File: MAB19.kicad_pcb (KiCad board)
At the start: 2 copper layers, 84 parts, among them J1 Screw_Terminal_01x02, J2 Screw_Terminal_01x03, J401 USART, J601 RJ45, J602 RJ45, K1 coil: 12VDC, contact: 125V/10A, Q1 BCV27, U1 4N25, U201 MCP2551-I/SN, U202 MCP2515-xSO, U401 ATMEGA328P-PU, U501 LM7805, Y201 16MHz, Y401 16MHz

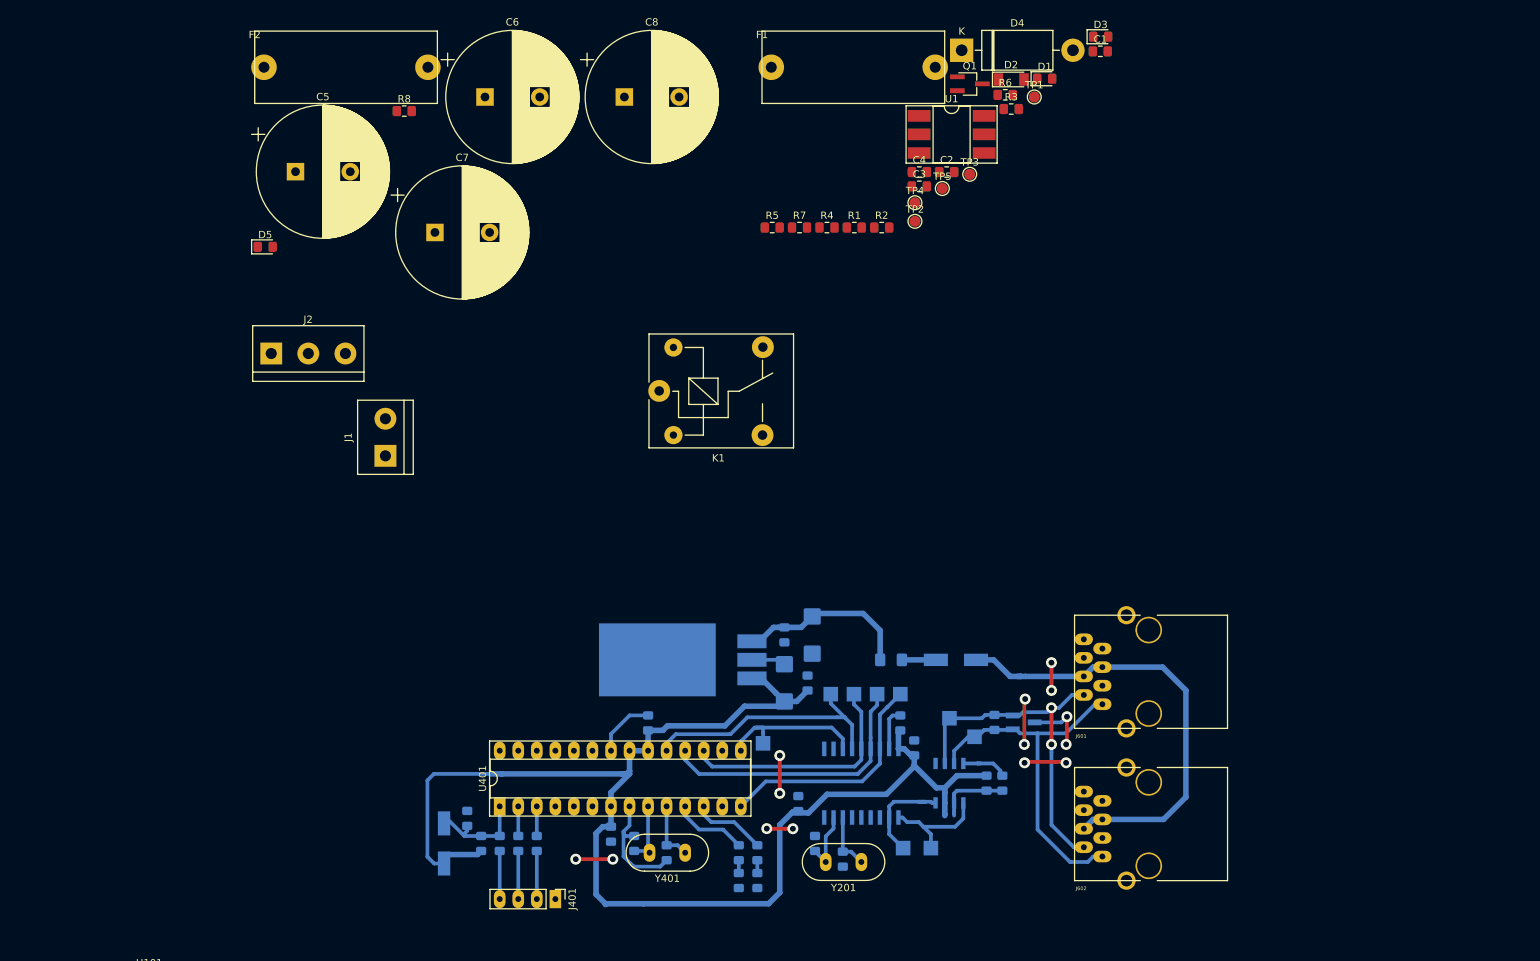
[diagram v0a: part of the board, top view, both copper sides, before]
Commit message: Adicionado safe zone para separar os GNDs
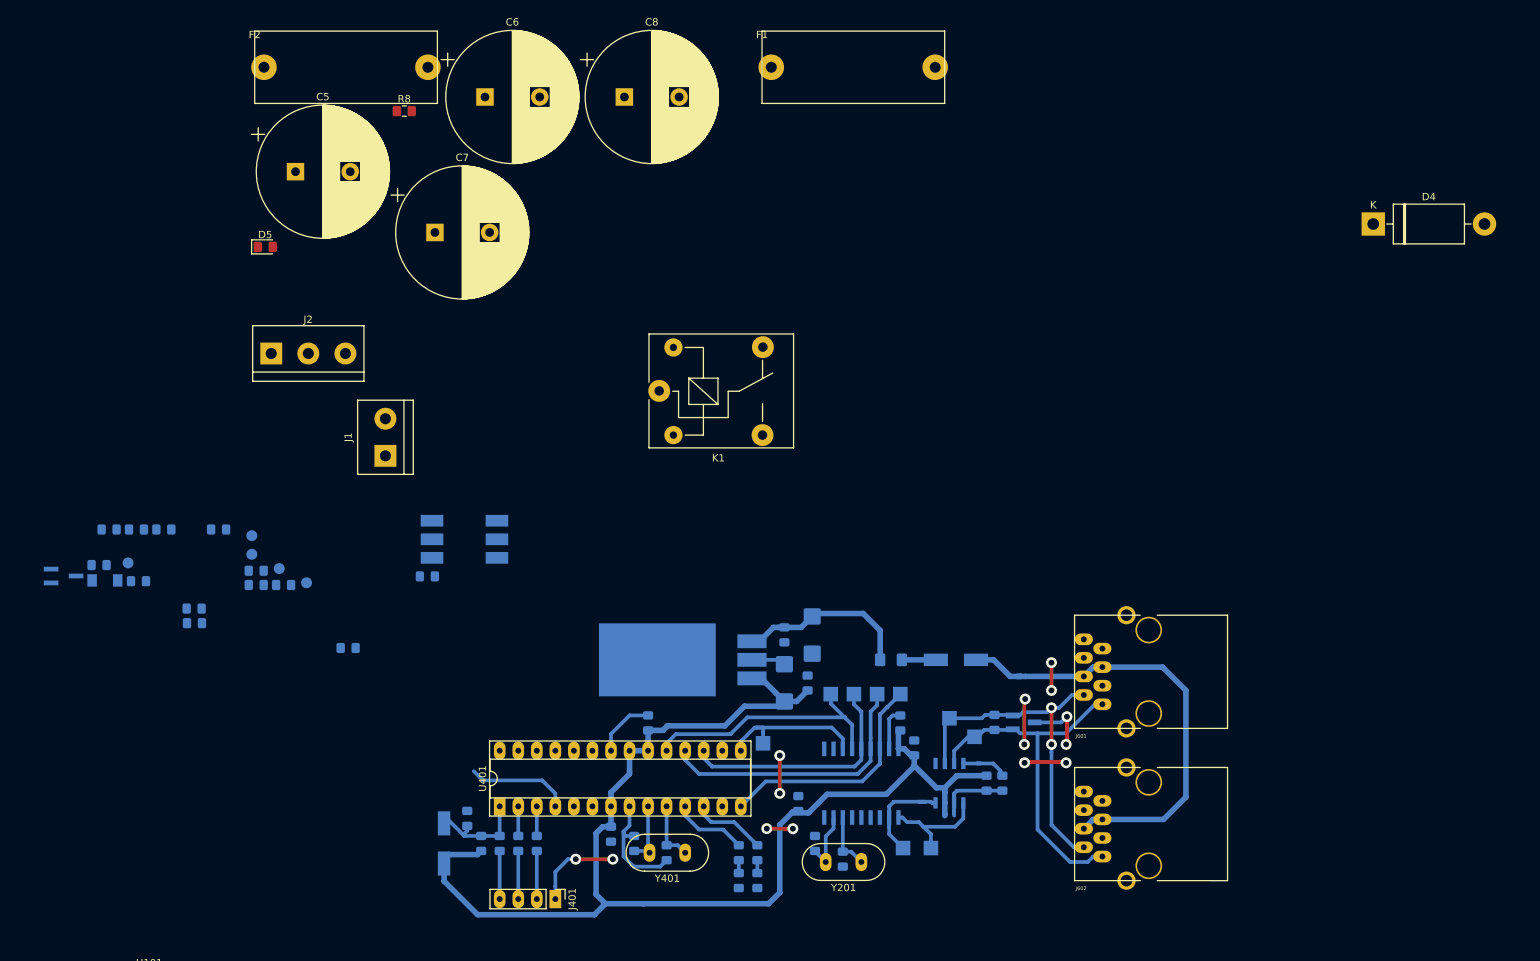
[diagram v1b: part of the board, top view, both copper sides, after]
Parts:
- C1, C2, C3, C4, D1, D2, D3, Q1, R1, R2, R3, R4, R5, R6, R7, TP1, TP2, TP3, TP4, TP5, U1: moved to B.Cu
- moved D3 147.8 mm to (68.4, 82.6)
- moved C1 145.7 mm to (68.4, 80.6)
- moved D1 141.9 mm to (60.8, 76.9)
- moved D2 141.8 mm to (56.2, 76.7)
- moved Q1 141.2 mm to (50.5, 76.1)
- moved R6 139.8 mm to (55.4, 74.6)
- moved TP1 139.5 mm to (59.3, 74.3)
- moved R3 117.0 mm to (89.5, 86.0)
- moved C2 107.0 mm to (80.6, 77.4)
- moved C4 107.0 mm to (76.9, 77.4)
- moved TP3 106.7 mm to (83.8, 77.1)
- moved C3 105.0 mm to (76.9, 75.4)
- moved TP5 104.7 mm to (80.0, 75.1)
- moved TP4 102.8 mm to (76.3, 73.2)
- moved TP2 100.5 mm to (76.3, 70.6)
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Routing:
- net +5V: track 187.6 -> 170.6 mm
- net /MCU/ON_OFF_PUMP: track 0.00 -> 14.2 mm
- net GND: track 79.5 -> 86.8 mm

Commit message: Pequena alteeração
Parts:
- moved TP1 62.8 mm to (119.4, 92.7)
- moved TP2 51.9 mm to (121.9, 95.2)
- moved C1 50.6 mm to (116.8, 95.2), turned to 270 degrees
- moved R1 20.0 mm to (105.4, 95.5), turned to 270 degrees
- moved U1 18.9 mm to (111.8, 88.9), turned to 90 degrees
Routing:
- net Net-(C1-Pad1): track 0.00 -> 21.7 mm
- net GND: track 86.8 -> 106.8 mm
- net /MCU/ON_OFF_PUMP: track 14.2 -> 21.1 mm
- added copper zone on B.Cu, net GND

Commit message: First version PCB
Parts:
- added JP1: SolderJumper_3_Bridged12, Jumper:SolderJumper-3_P1.3mm_Bridged2Bar12_Pad1.0x1.5mm_NumberLabels, B.Cu at (118.1, 64.1)
- D5, R8: moved to B.Cu
- moved F2 133.6 mm to (200.7, 51.2), turned to 180 degrees
- moved D5 125.9 mm to (202.6, 50.2), turned to 90 degrees
- moved R8 113.5 mm to (202.6, 54.6), turned to 90 degrees
- moved D4 102.6 mm to (128.9, 46.4), turned to 180 degrees
- moved C5 101.0 mm to (172.5, 66.0), turned to 90 degrees
- moved C8 86.0 mm to (193.0, 66.0), turned to 90 degrees
- moved C7 62.7 mm to (152.0, 66.0), turned to 90 degrees
- moved C6 60.2 mm to (131.4, 66.0), turned to 90 degrees
- moved Q1 58.5 mm to (106.7, 59.7)
- moved F1 56.1 mm to (172.1, 51.2), turned to 180 degrees
- moved R6 51.1 mm to (102.9, 55.9), turned to 90 degrees
- moved J1 49.2 mm to (141.0, 43.2), turned to 180 degrees
- moved D3 48.1 mm to (104.1, 50.4), turned to 90 degrees
- moved D2 47.3 mm to (101.0, 61.6), turned to 90 degrees
- moved R5 44.6 mm to (101.0, 75.3), turned to 270 degrees
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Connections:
- net /POWER SUPPLY/+18V_OUT renamed Net-(C501-Pad1)
- J1 pad 1: GNDPWR -> /filter/Vin
- J1 pad 2: /filter/Vin -> GNDPWR
- K1 pad 3: /pump_driver/+Pump -> Net-(JP1-Pad1)
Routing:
- net GNDPWR: track 0.00 -> 201.2 mm
- net /pump_driver/Level_sensor: track 0.00 -> 131.9 mm
- net +12V: track 0.00 -> 129.5 mm
- net /pump_driver/+Pump: track 0.00 -> 62.0 mm
- net /filter/Vin: track 0.00 -> 43.3 mm
- net Net-(C4-Pad1): track 0.00 -> 26.8 mm
- net Net-(JP1-Pad3): track 0.00 -> 13.4 mm
- net Net-(C3-Pad1): track 0.00 -> 11.1 mm
- net Net-(D2-Pad2): track 0.00 -> 9.47 mm
- net Net-(JP1-Pad1): track 0.00 -> 7.32 mm
- net Net-(C2-Pad2): track 0.00 -> 6.59 mm
- net Net-(D3-Pad1): track 0.00 -> 4.66 mm
- net Net-(D1-Pad1): track 0.00 -> 4.48 mm
- net Net-(Q1-Pad2): track 0.00 -> 3.68 mm
- net Net-(C1-Pad1): track 21.7 -> 24.2 mm
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- added copper zone on B.Cu, net GNDPWR
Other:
- net class power added: clearance 0.762, trace_width 1.524, via_dia 1.5, via_drill 0.8

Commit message: Foram reorganizadas algumas zonas para diminuir as dimensoes
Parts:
- moved H103 77.7 mm to (203.2, 42.8)
- moved H104 74.8 mm to (90.2, 42.8)
- moved Q1 6.38 mm to (106.0, 66.0)
- moved F1 6.38 mm to (171.4, 57.6)
- moved D1 6.38 mm to (93.3, 56.8)
- moved D3 6.38 mm to (103.5, 56.8)
- moved J2 6.38 mm to (105.4, 49.5)
- moved K1 6.38 mm to (96.5, 67.3)
- moved R4 6.38 mm to (97.0, 56.8)
- moved R7 6.38 mm to (99.7, 56.8)
- moved D4 6.38 mm to (128.3, 52.7)
- moved D5 6.38 mm to (201.9, 56.5)
- moved F2 6.38 mm to (200.0, 57.6)
- moved J1 6.38 mm to (140.3, 49.5)
- moved R8 6.38 mm to (201.9, 61.0)
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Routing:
- net GNDPWR: track 201.2 -> 195.8 mm
- net Net-(C3-Pad1): track 11.1 -> 14.6 mm
- net Net-(C4-Pad1): track 26.8 -> 25.9 mm

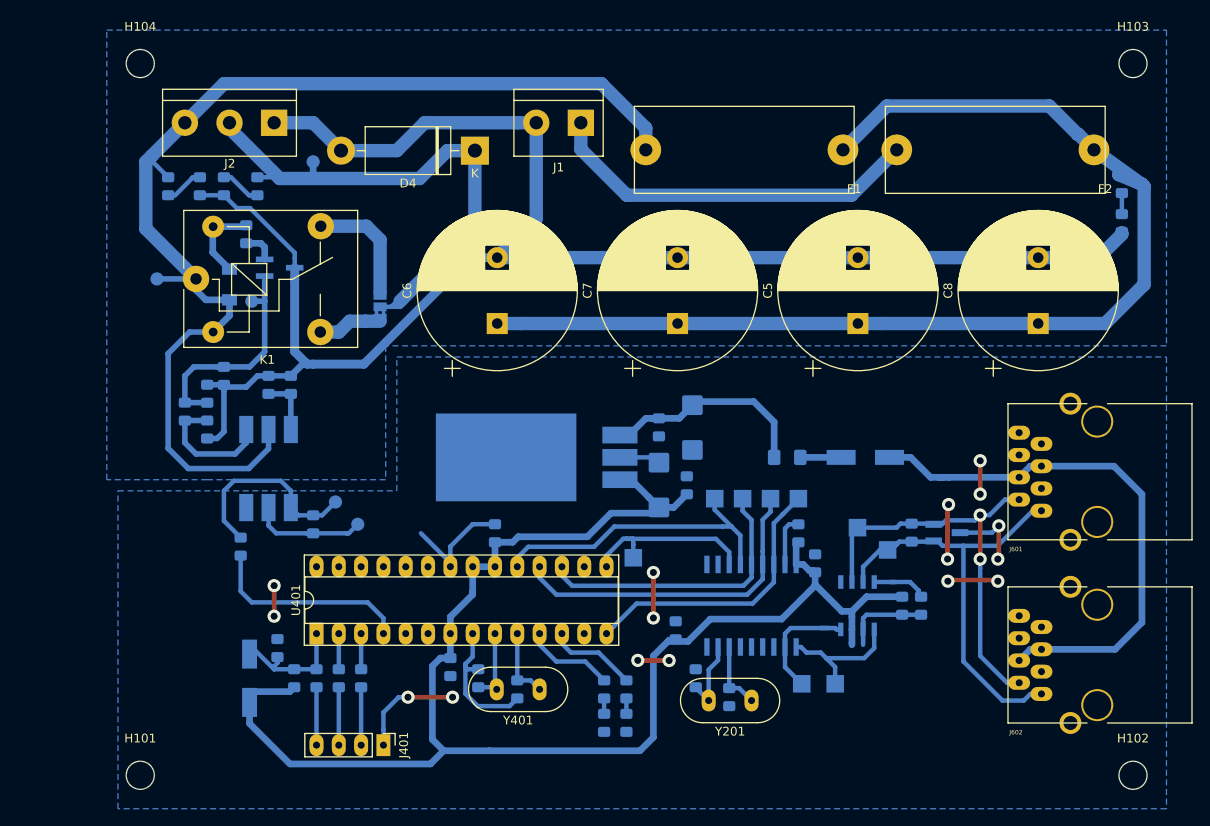
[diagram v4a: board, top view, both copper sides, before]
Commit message: Foram reposicionados os conectores Pois onde eles estavam não permitiam que ouvese uma placa igual do lado
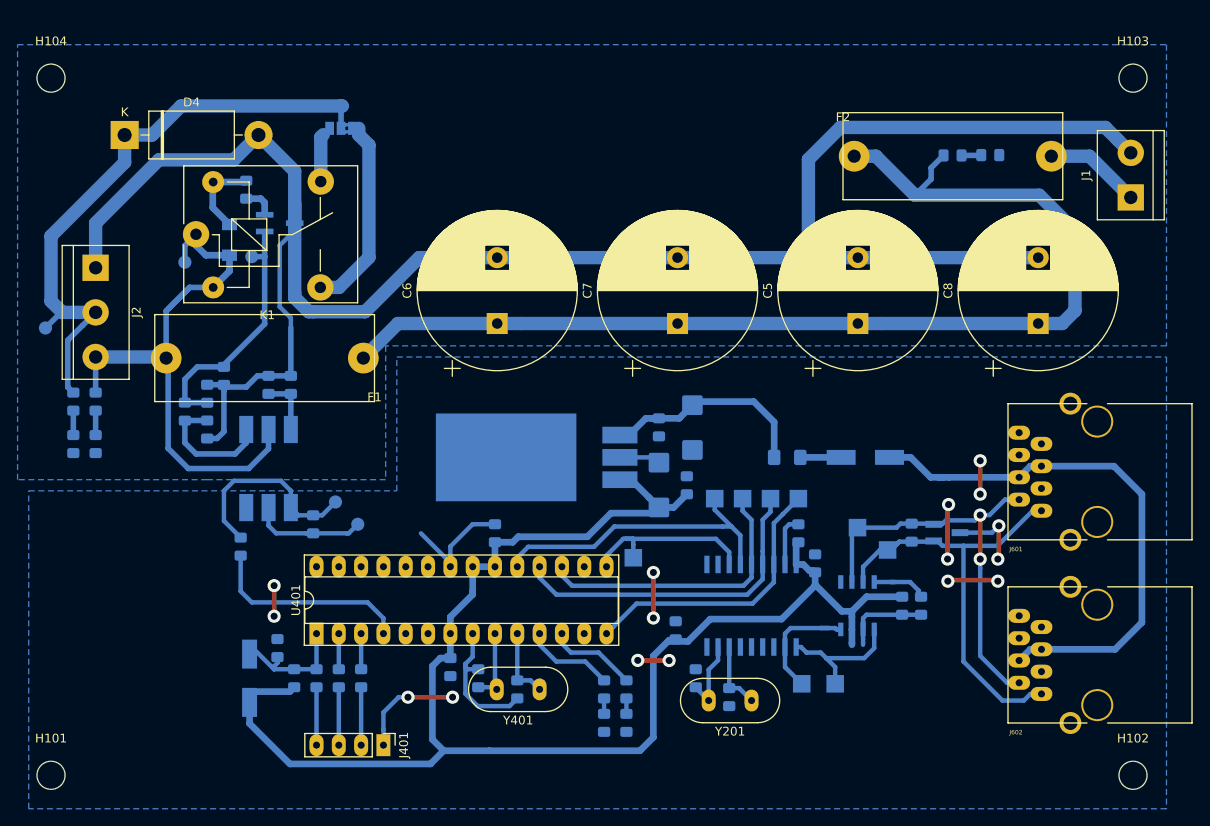
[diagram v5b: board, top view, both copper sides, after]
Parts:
- moved J1 63.2 mm to (202.9, 58.0), turned to 90 degrees
- moved F1 59.5 mm to (116.8, 81.3)
- moved D4 39.9 mm to (88.4, 50.9), turned to 0 degrees
- moved TP5 35.9 mm to (79.4, 72.9)
- moved R7 34.0 mm to (82.5, 86.1)
- moved D3 32.3 mm to (82.5, 81.3)
- moved R4 31.7 mm to (85.1, 86.1)
- moved F2 31.2 mm to (170.2, 48.4), turned to 0 degrees
- moved J2 26.2 mm to (85.1, 66.0), turned to 270 degrees
- moved D1 25.9 mm to (85.1, 81.3)
- moved JP1 20.8 mm to (113.0, 50.2), turned to 180 degrees
- moved D5 19.5 mm to (182.7, 53.3), turned to 180 degrees
- moved R8 16.9 mm to (186.9, 53.2), turned to 180 degrees
- moved H104 10.3 mm to (80.0, 44.5)
- moved H101 10.2 mm to (80.0, 123.8)
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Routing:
- net /pump_driver/Level_sensor: track 131.9 -> 68.4 mm
- net GNDPWR: track 195.8 -> 231.7 mm
- net /filter/Vin: track 43.3 -> 11.0 mm
- net Net-(JP1-Pad1): track 7.32 -> 22.1 mm
- net /pump_driver/+Pump: track 62.0 -> 69.5 mm
- net Net-(JP1-Pad3): track 13.4 -> 6.18 mm
- net Net-(C4-Pad1): track 25.9 -> 29.0 mm
- net +12V: track 129.5 -> 126.9 mm
- net Net-(D3-Pad1): track 4.66 -> 2.78 mm
- net Net-(D1-Pad1): track 4.48 -> 2.78 mm

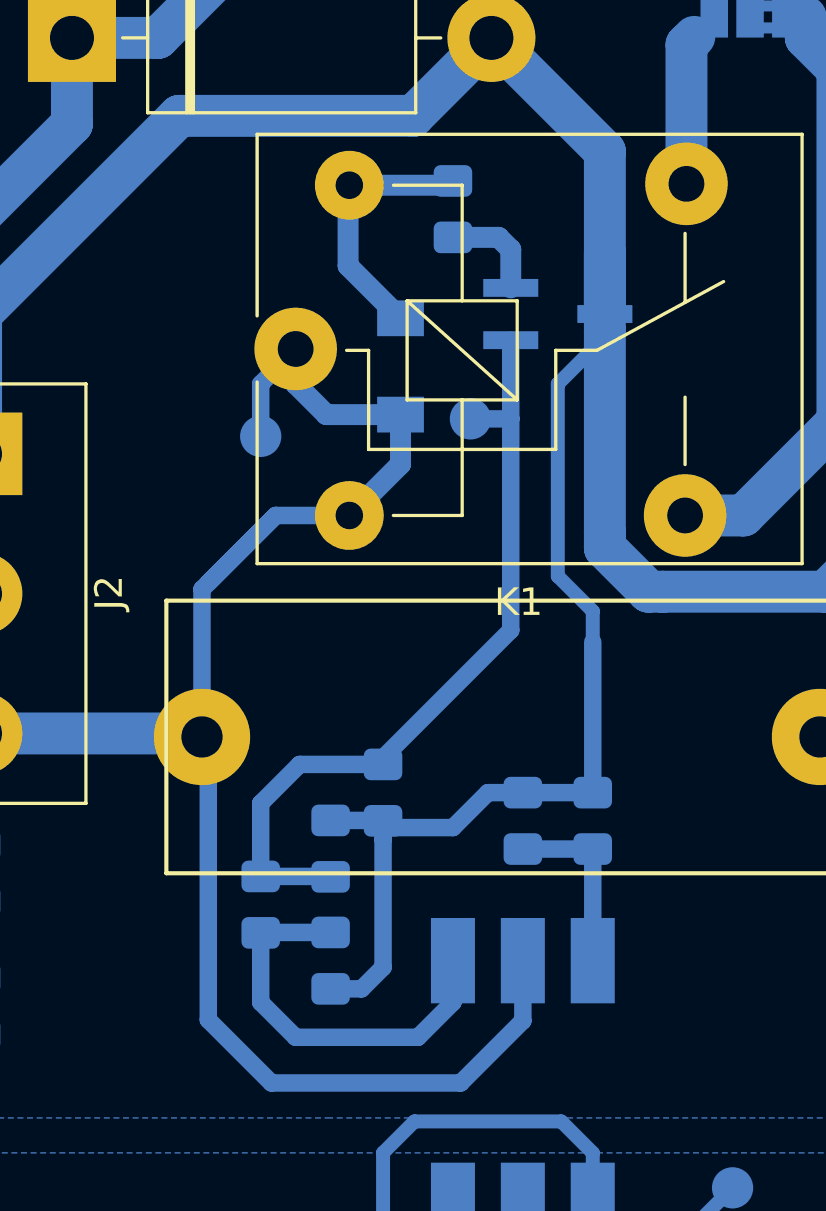
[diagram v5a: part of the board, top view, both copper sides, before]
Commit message: Solucionado erro na disposição dos pinos do BCV27
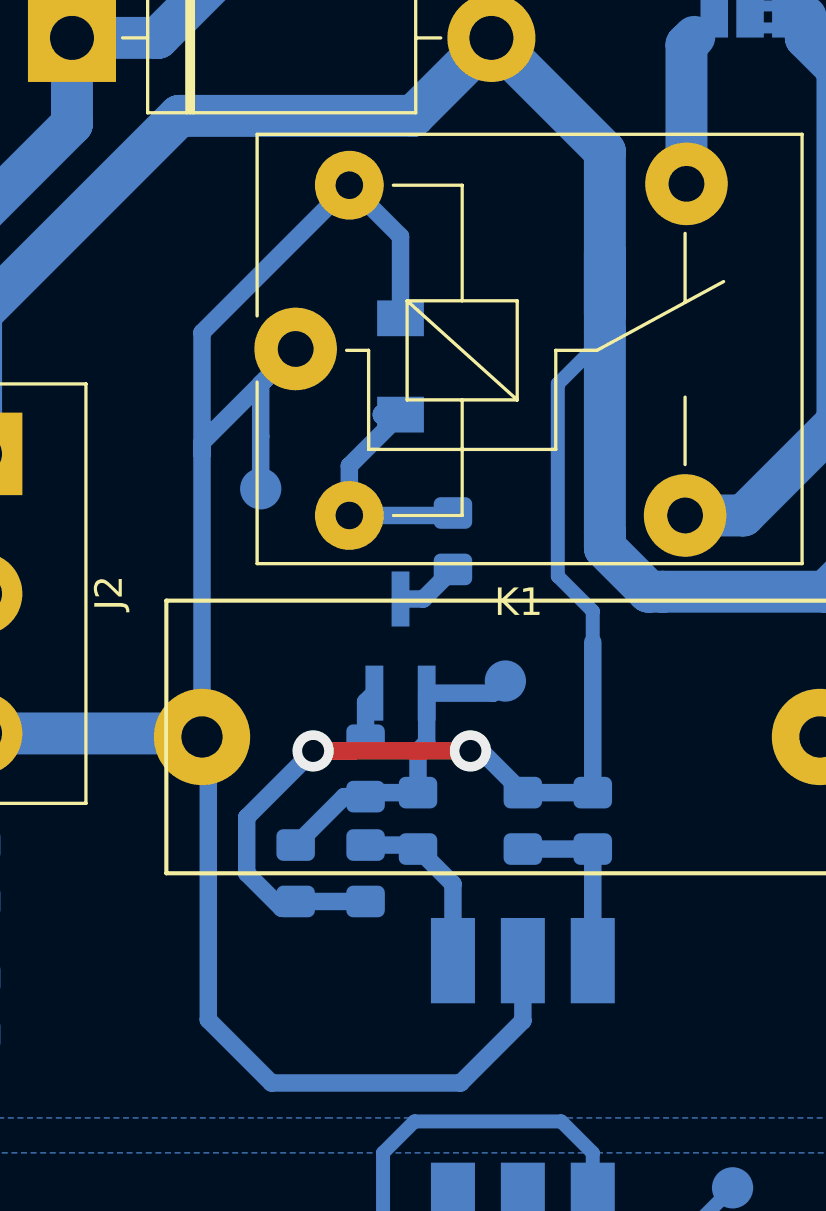
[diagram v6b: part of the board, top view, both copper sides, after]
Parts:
- Q1: value BCV27 -> Q_NPN_BEC
- moved Q1 13.4 mm to (100.3, 73.0), turned to 90 degrees
- moved R6 12.1 mm to (102.2, 69.2)
- moved TP4 9.61 mm to (104.1, 74.3)
- moved R3 6.48 mm to (101.0, 79.4)
- moved C3 3.42 mm to (99.1, 81.3)
- moved TP3 1.91 mm to (95.2, 67.3)
- moved R5 1.55 mm to (96.5, 81.3), turned to 90 degrees
- moved C4 1.09 mm to (99.1, 77.5), turned to 90 degrees
- turned D2 to 270 degrees
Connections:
- K1 pad 2: /pump_driver/Level_sensor -> Net-(D2-Pad2)
- K1 pad 5: Net-(D2-Pad2) -> /pump_driver/Level_sensor
- Q1 pad 2: Net-(Q1-Pad2) -> GNDPWR
- Q1 pad 3: GNDPWR -> Net-(Q1-Pad3)
- R6 pad 1: Net-(Q1-Pad2) -> Net-(Q1-Pad3)
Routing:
- net Net-(C4-Pad1): track 29.0 -> 12.0 mm
- net /pump_driver/Level_sensor: track 68.4 -> 77.1 mm
- net Net-(C3-Pad1): track 14.6 -> 6.55 mm
- net GNDPWR: track 231.7 -> 239.1 mm, vias 0 -> 2
- net Net-(Q1-Pad2): track 3.68 -> 0.00 mm
- net Net-(Q1-Pad3): track 0.00 -> 2.35 mm
